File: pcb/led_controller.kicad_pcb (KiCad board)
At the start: 2 copper layers, 72 parts, among them IC1 ATTINY2313A-S, P1 POSITIVE_OUT_1, P10 NEGATIVE_OUT_1, P11 NEGATIVE_OUT_2, P12 NEGATIVE_OUT_2, P13 NEGATIVE_OUT_2, P14 ISP, P15 +12v IN, P16 GND IN, P2 POSITIVE_OUT_2, P3 POSITIVE_OUT_3, P4 POSITIVE_OUT_4, P5 ESP8266, P6 POSITIVE_OUT_5, P7 POSITIVE_OUT_6, P8 NEGATIVE_OUT_1, P9 NEGATIVE_OUT_1, Q1 MOSFET_P, Q10 MOSFET_N, Q2 MOSFET_P, Q3 MOSFET_P, Q4 MOSFET_P, Q5 MOSFET_P, Q6 MOSFET_P, Q7 BS170, Q8 BS170, Q9 MOSFET_N, SW1 B1, SW2 B2, U1 TC4426A, U2 TC4426A, U3 TC4426A, U4 TC4427A, U5 MCP1700, U6 MC34063, X1 20MHz

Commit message: position power supply
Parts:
- added P17: +12v OUT, connectors:1PIN_DG306, F.Cu at (214.6, 85.7)
- added P18: GND OUT, connectors:1PIN_DG306, F.Cu at (209.6, 85.7)
- moved P15 177.0 mm to (214.0, 100.0), turned to 270 degrees
- moved P16 177.0 mm to (214.0, 94.9), turned to 270 degrees
- moved C5 154.6 mm to (202.2, 97.5)
- moved R21 146.8 mm to (201.0, 112.1), turned to 180 degrees
- moved C6 144.5 mm to (206.7, 117.2), turned to 0 degrees
- moved R18 143.6 mm to (197.2, 112.7), turned to 270 degrees
- moved R22 143.6 mm to (201.0, 114.6), turned to 180 degrees
- moved R17 140.4 mm to (201.0, 117.2), turned to 180 degrees
- moved R20 138.0 mm to (211.8, 126.0), turned to 270 degrees
- moved R19 135.4 mm to (208.6, 126.0), turned to 90 degrees
- moved U6 131.1 mm to (201.0, 124.8), turned to 0 degrees
- moved C11 124.6 mm to (208.6, 135.6), turned to 0 degrees
- moved C4 123.9 mm to (155.9, 172.4)
- moved C10 123.9 mm to (145.7, 172.4)
- moved C3 123.9 mm to (155.9, 174.9)
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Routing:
- net GND: track 171.4 -> 210.0 mm
- net Net-(Q9-PadG): track 14.2 -> 33.6 mm
- net VDD: track 125.7 -> 143.1 mm

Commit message: arrange everything
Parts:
- removed R14: 10k, Resistors_SMD:R_0805
- C8: footprint Capacitors_ThroughHole:Capacitor6MMDiscRM5 -> Capacitors_SMD:C_0805; moved to B.Cu
- R9: footprint Resistors_SMD:R_0805 -> Resistors_ThroughHole:Resistor_Horizontal_RM10mm; moved to F.Cu
- moved U5 59.2 mm to (193.0, 151.1)
- moved C9 53.0 mm to (194.3, 143.5), turned to 90 degrees
- moved C4 48.8 mm to (201.0, 153.7)
- moved C10 46.2 mm to (188.0, 153.7)
- moved C3 45.8 mm to (187.6, 141.9), turned to 270 degrees
- moved R9 25.5 mm to (168.9, 138.7), turned to 180 degrees
- moved R20 18.2 mm to (206.7, 108.6), turned to 90 degrees
- moved C11 16.0 mm to (210.5, 119.7), turned to 90 degrees
- moved D3 10.1 mm to (206.4, 130.5)
- moved C7 9.86 mm to (201.6, 139.1)
- moved L1 9.47 mm to (193.7, 132.1)
- moved C6 7.10 mm to (203.5, 110.8), turned to 90 degrees
- moved R17 4.26 mm to (199.1, 113.3)
- moved R18 4.26 mm to (195.3, 108.9)
- moved R19 4.26 mm to (206.7, 122.2)
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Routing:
- net +5V: track 39.6 -> 71.1 mm
- net +3V3: track 36.4 -> 65.4 mm, vias 0 -> 2
- net GND: track 210.0 -> 223.6 mm
- net VDD: track 143.1 -> 150.1 mm
- net /RX_WIFI: track 38.3 -> 44.1 mm
- net /RX_AVR: track 17.4 -> 20.6 mm
- net Net-(C11-Pad1): track 9.31 -> 12.1 mm
- net /RESET: track 33.6 -> 34.3 mm

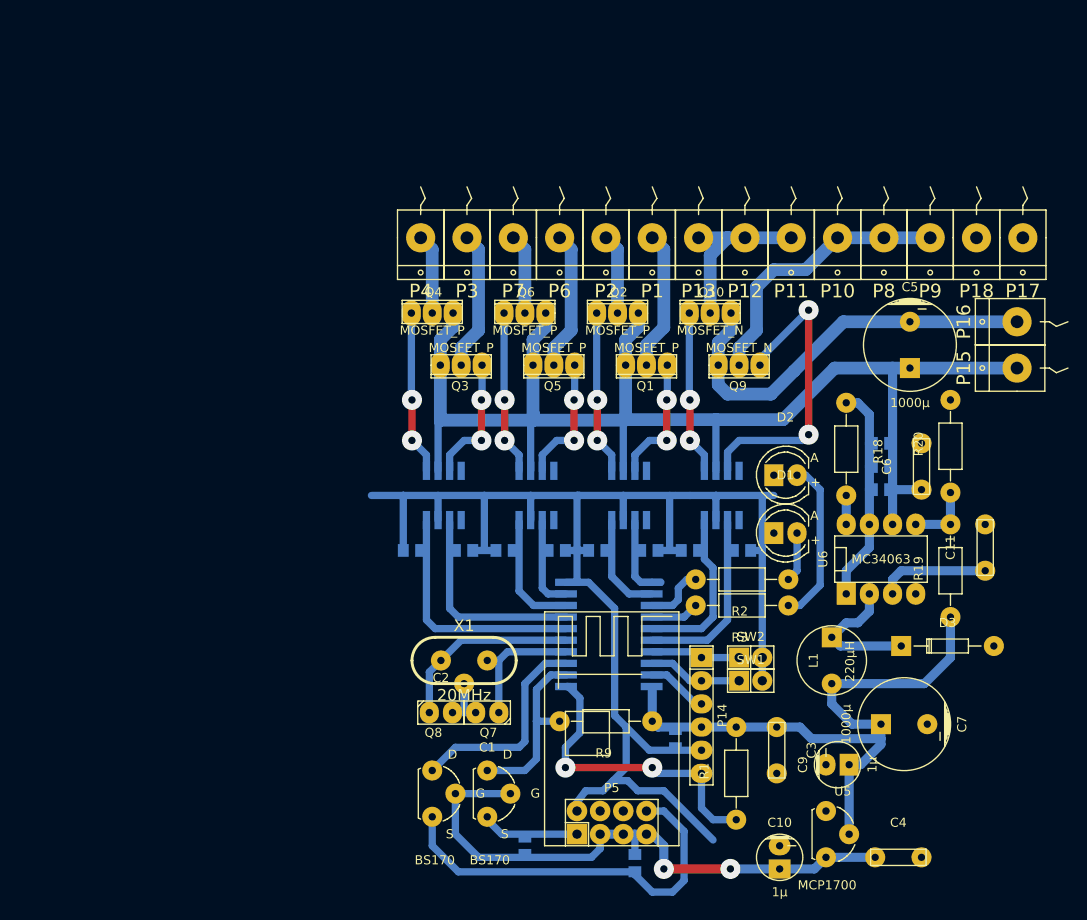
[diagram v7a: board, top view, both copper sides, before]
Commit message: add power planes
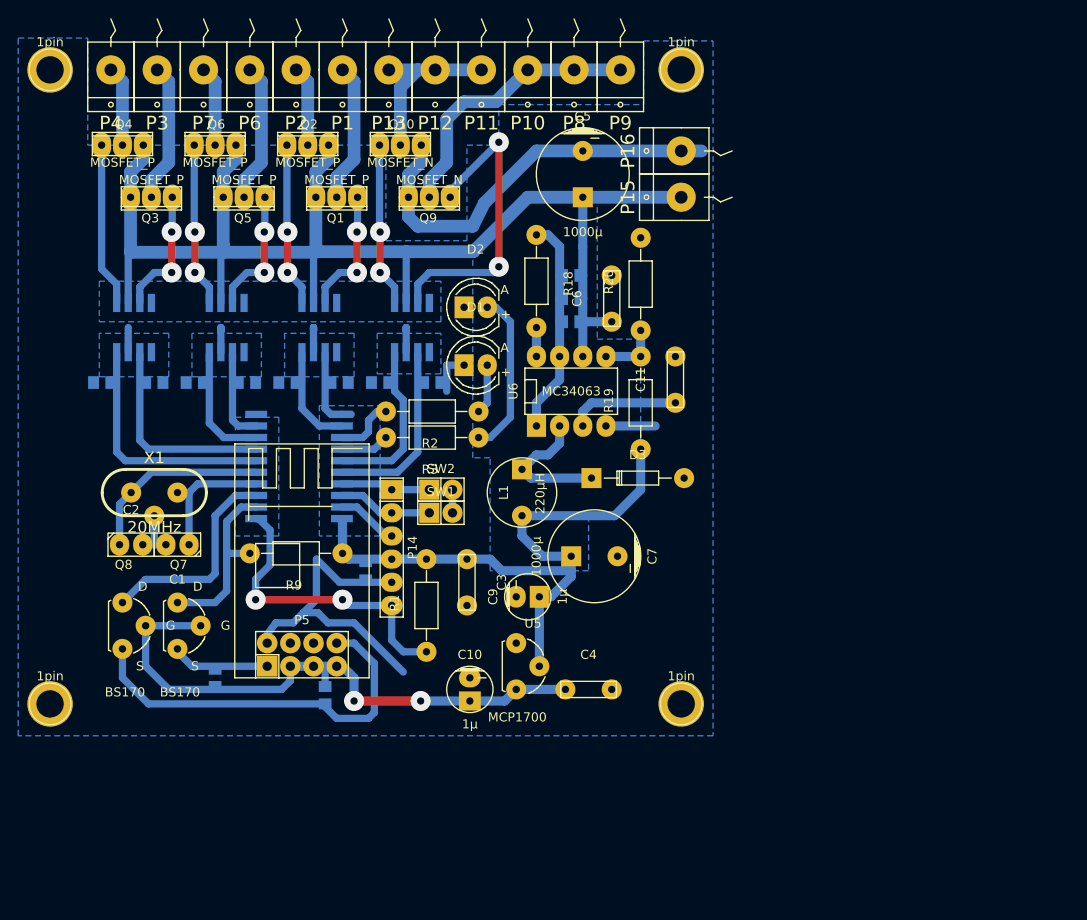
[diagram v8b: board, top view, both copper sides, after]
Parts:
- removed P17: +12v OUT, connectors:1PIN_DG306
- removed P18: GND OUT, connectors:1PIN_DG306
- added 1pin: VAL**, Connect:1pin, F.Cu at (177.2, 136.8)
- added 1pin: VAL**, Connect:1pin, F.Cu at (108.0, 136.8)
- added 1pin: VAL**, Connect:1pin, F.Cu at (108.0, 67.3)
- added 1pin: VAL**, Connect:1pin, F.Cu at (177.2, 67.3)
- moved P15 41.3 mm to (177.2, 81.3)
- moved P16 41.3 mm to (177.2, 76.2)
- moved C5 40.5 mm to (166.4, 78.7)
- moved C3 38.6 mm to (153.7, 123.5)
- moved C6 38.6 mm to (169.5, 92.4)
- moved L1 38.6 mm to (159.7, 113.7)
- moved R4 38.6 mm to (139.7, 101.6)
- moved U4 38.6 mm to (147.6, 95.6)
- moved C7 38.6 mm to (167.6, 120.7)
- moved P6 38.6 mm to (129.9, 67.3)
- moved Q4 38.6 mm to (115.9, 75.6)
- moved Q6 38.6 mm to (126.0, 75.6)
- moved R12 38.6 mm to (123.8, 101.6)
- moved C1 38.6 mm to (121.9, 119.4)
- moved P5 38.6 mm to (135.6, 131.4)
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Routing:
- net GND: track 223.6 -> 112.1 mm
- net VDD: track 150.1 -> 147.7 mm
- net Net-(R19-Pad2): track 7.30 -> 6.67 mm
- net /RX_WIFI: track 44.1 -> 43.5 mm
- net Net-(Q4-PadG): vias 2 -> 0
- added copper zone on B.Cu, net GND
